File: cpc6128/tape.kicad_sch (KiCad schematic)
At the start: 60 parts, among them IC301 LA4140, IC302 LA6358S, J301 +5V, J306 TAPE_PORT, Q101 2SC2120Y, Q301 KTC1815Y, Q302 Q_NPN_ECB, Q303 Q_PNP_ECB

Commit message: Update title blocks
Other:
- company: (none) -> Amstrad plc
- title: Tape/Sound/Power -> CPC6128 MC0020x tape audio and power
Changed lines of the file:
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@@
   (paper "A3")
   (title_block
-    (title "Tape/Sound/Power")
+    (title "CPC6128 MC0020x tape audio and power")
+    (date "2022-08-20")
+    (rev "1")
+    (company "Amstrad plc")
   )
   (junction (at 83.82 104.775) (diameter 0) (color 0 0 0 0)

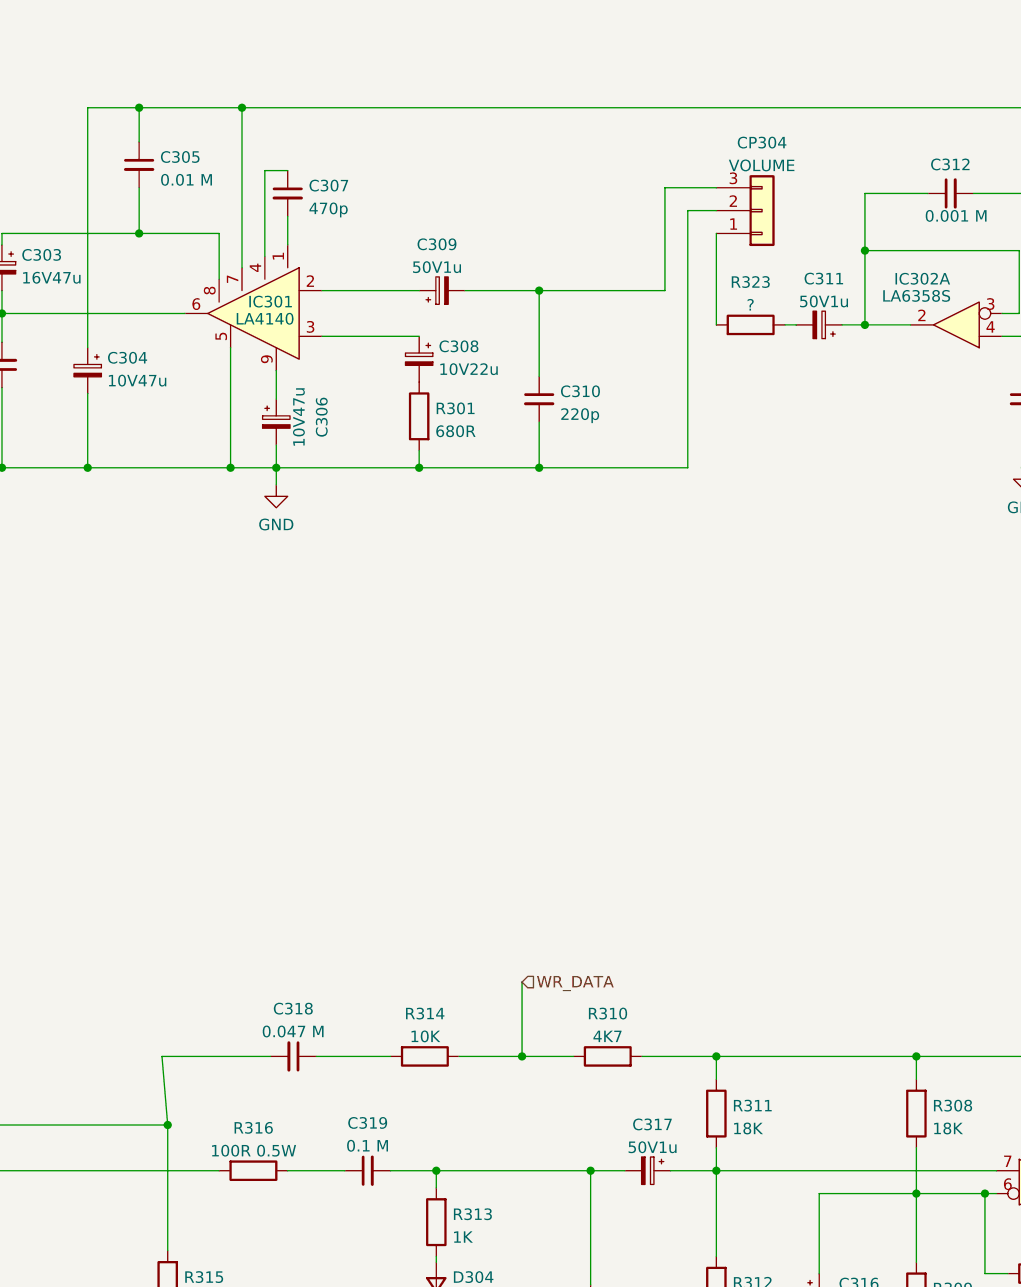
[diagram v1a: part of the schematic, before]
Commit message: Fixes from new top pcb image
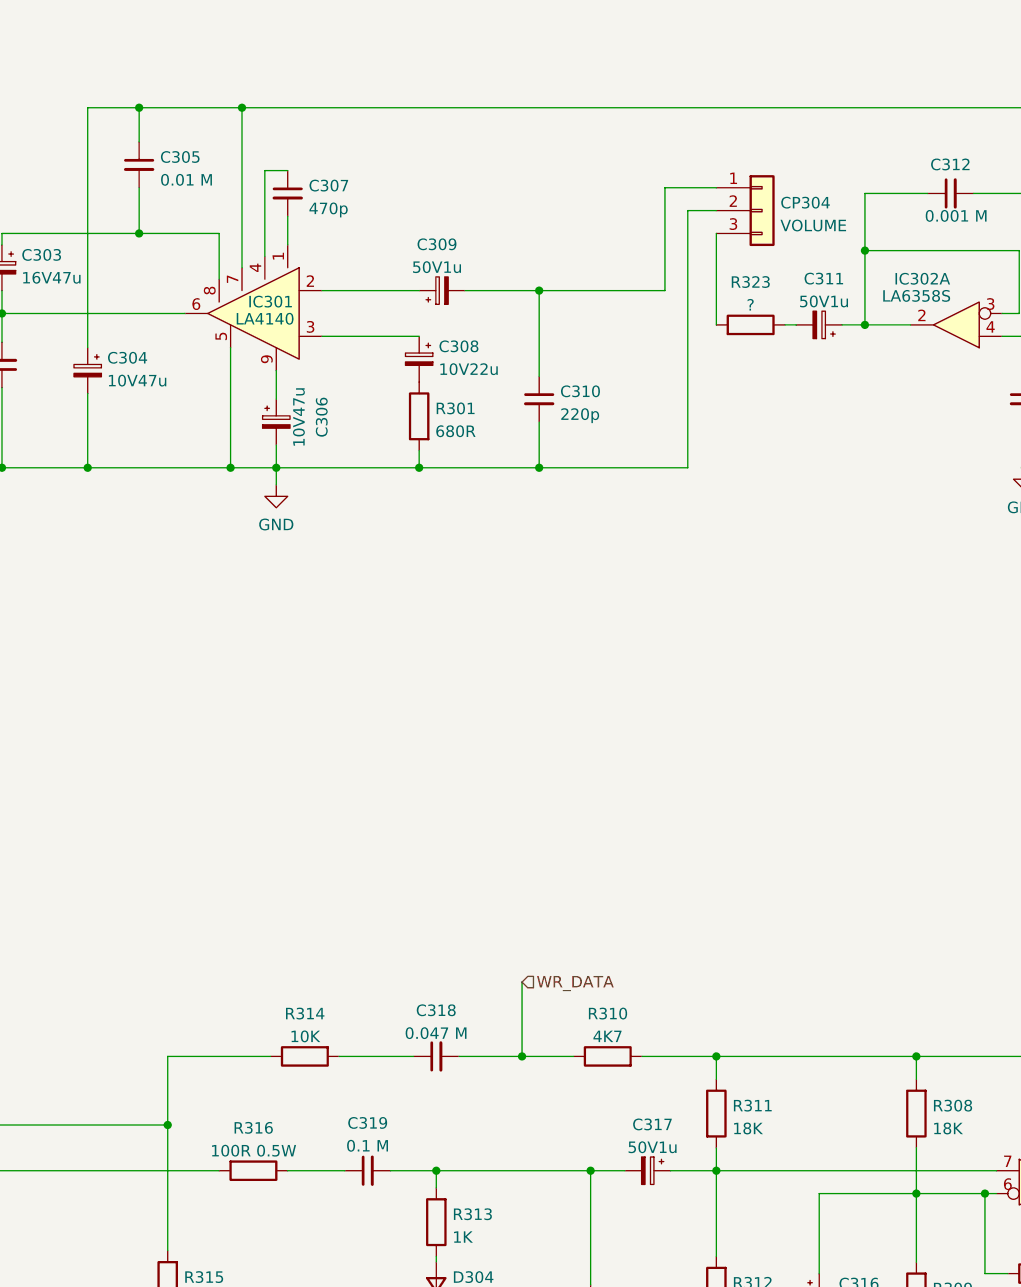
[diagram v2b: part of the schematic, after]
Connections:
- net EAR: now also R314.1; no longer C318.2
- net WR_DATA: now also C318.2; no longer R314.1
- net at C309.2, C310.1: now also CP304.1 (Pin_1); no longer CP304.3 (Pin_3)
- net at R323.2: now also CP304.3 (Pin_3); no longer CP304.1 (Pin_1)
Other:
- moved on the sheet: C318, R314
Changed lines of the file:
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@@
     (stroke (width 0) (type default) (color 0 0 0 0))
   )
-  (wire (pts (xy 109.22 170.18) (xy 117.475 170.18))
+  (wire (pts (xy 111.76 170.18) (xy 120.015 170.18))
     (stroke (width 0) (type default) (color 0 0 0 0))
   )
@@
     (stroke (width 0) (type default) (color 0 0 0 0))
   )
+  (wire (pts (xy 92.71 170.18) (xy 104.14 170.18))
+    (stroke (width 0) (type default) (color 0 0 0 0))
+  )
   (wire (pts (xy 153.67 182.88) (xy 153.67 192.405))
     (stroke (width 0) (type default) (color 0 0 0 0))
@@
     (stroke (width 0) (type default) (color 0 0 0 0))
   )
-  (wire (pts (xy 92.71 177.8) (xy 92.075 170.18))
+  (wire (pts (xy 92.71 177.8) (xy 92.71 170.18))
     (stroke (width 0) (type default) (color 0 0 0 0))
   )
@@
   )
   (wire (pts (xy 43.815 195.58) (xy 43.815 201.93))
-    (stroke (width 0) (type default) (color 0 0 0 0))
-  )
-  (wire (pts (xy 92.075 170.18) (xy 104.14 170.18))
     (stroke (width 0) (type default) (color 0 0 0 0))
   )
@@
     (pin "1")
   )
-  (symbol (lib_id "Device:R") (at 121.285 170.18 270) (unit 1)
-    (in_bom yes) (on_board yes) (fields_autoplaced)
-    (property "Reference" "R314" (id 0) (at 121.285 165.4642 90))
-    (property "Value" "10K" (id 1) (at 121.285 168.0011 90))
-    (property "Footprint" "Resistor_THT:R_Axial_DIN0207_L6.3mm_D2.5mm_P10.16mm_Horizontal" (id 2) (at 121.285 168.402 90)
-      (effects (font (size 1.27 1.27)) hide)
-    )
-    (property "Datasheet" "~" (id 3) (at 121.285 170.18 0)
+  (symbol (lib_id "Device:R") (at 107.95 170.18 90) (mirror x) (unit 1)
+    (in_bom yes) (on_board yes) (fields_autoplaced)
+    (property "Reference" "R314" (id 0) (at 107.95 165.4642 90))
+    (property "Value" "10K" (id 1) (at 107.95 168.0011 90))
+    (property "Footprint" "Resistor_THT:R_Axial_DIN0207_L6.3mm_D2.5mm_P10.16mm_Horizontal" (id 2) (at 107.95 168.402 90)
+      (effects (font (size 1.27 1.27)) hide)
+    )
+    (property "Datasheet" "~" (id 3) (at 107.95 170.18 0)
       (effects (font (size 1.27 1.27)) hide)
     )
@@
     (pin "1")
   )
-  (symbol (lib_id "Device:C_Small") (at 106.68 170.18 270) (unit 1)
+  (symbol (lib_id "Device:C_Small") (at 122.555 170.18 90) (unit 1)
     (in_bom yes) (on_board yes)
-    (property "Reference" "C318" (id 0) (at 106.6736 164.9181 90))
-    (property "Value" "0.047 M" (id 1) (at 106.6736 167.455 90))
-    (property "Footprint" "Capacitor_THT:C_Rect_L7.0mm_W2.0mm_P5.00mm" (id 2) (at 106.68 170.18 0)
-      (effects (font (size 1.27 1.27)) hide)
-    )
-    (property "Datasheet" "~" (id 3) (at 106.68 170.18 0)
+    (property "Reference" "C318" (id 0) (at 122.555 165.1 90))
+    (property "Value" "0.047 M" (id 1) (at 122.555 167.64 90))
+    (property "Footprint" "Capacitor_THT:C_Rect_L7.0mm_W2.0mm_P5.00mm" (id 2) (at 122.555 170.18 0)
+      (effects (font (size 1.27 1.27)) hide)
+    )
+    (property "Datasheet" "~" (id 3) (at 122.555 170.18 0)
       (effects (font (size 1.27 1.27)) hide)
     )
@@
     (pin "2")
   )
-  (symbol (lib_id "Connector_Generic:Conn_01x03") (at 158.75 76.2 0) (mirror x) (unit 1)
-    (in_bom yes) (on_board yes) (fields_autoplaced)
-    (property "Reference" "CP304" (id 0) (at 158.75 68.6902 0))
-    (property "Value" "VOLUME" (id 1) (at 158.75 71.2271 0))
+  (symbol (lib_id "Connector_Generic:Conn_01x03") (at 158.75 76.2 0) (unit 1)
+    (in_bom yes) (on_board yes) (fields_autoplaced)
+    (property "Reference" "CP304" (id 0) (at 160.782 75.3653 0)
+      (effects (font (size 1.27 1.27)) (justify left))
+    )
+    (property "Value" "VOLUME" (id 1) (at 160.782 77.9022 0)
+      (effects (font (size 1.27 1.27)) (justify left))
+    )
     (property "Footprint" "Connector_Molex:Molex_KK-254_AE-6410-03A_1x03_P2.54mm_Vertical" (id 2) (at 158.75 76.2 0)
       (effects (font (size 1.27 1.27)) hide)

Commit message: Minor cleanups
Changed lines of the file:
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@@
     (effects (font (size 1.27 1.27)) (justify left))
   )
-  (hierarchical_label "RD_DATA" (shape input) (at 198.12 184.15 0)
+  (hierarchical_label "RD_DATA" (shape output) (at 198.12 184.15 0)
     (effects (font (size 1.27 1.27)) (justify left))
   )

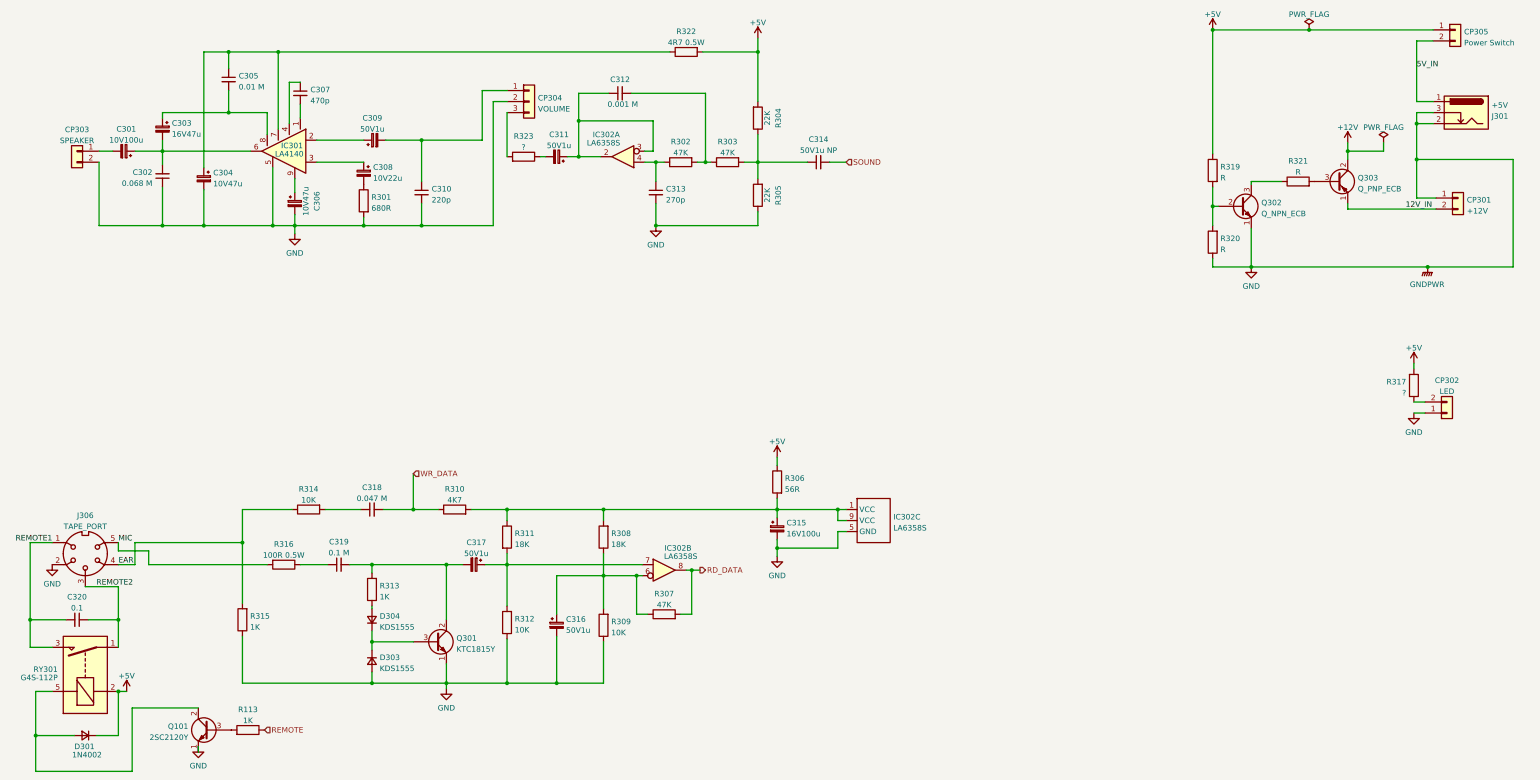
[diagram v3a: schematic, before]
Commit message: Correct C136 (missing) and C314 (wrong footprint) Thanks @orzel!
Also migrated to KiCad 9.
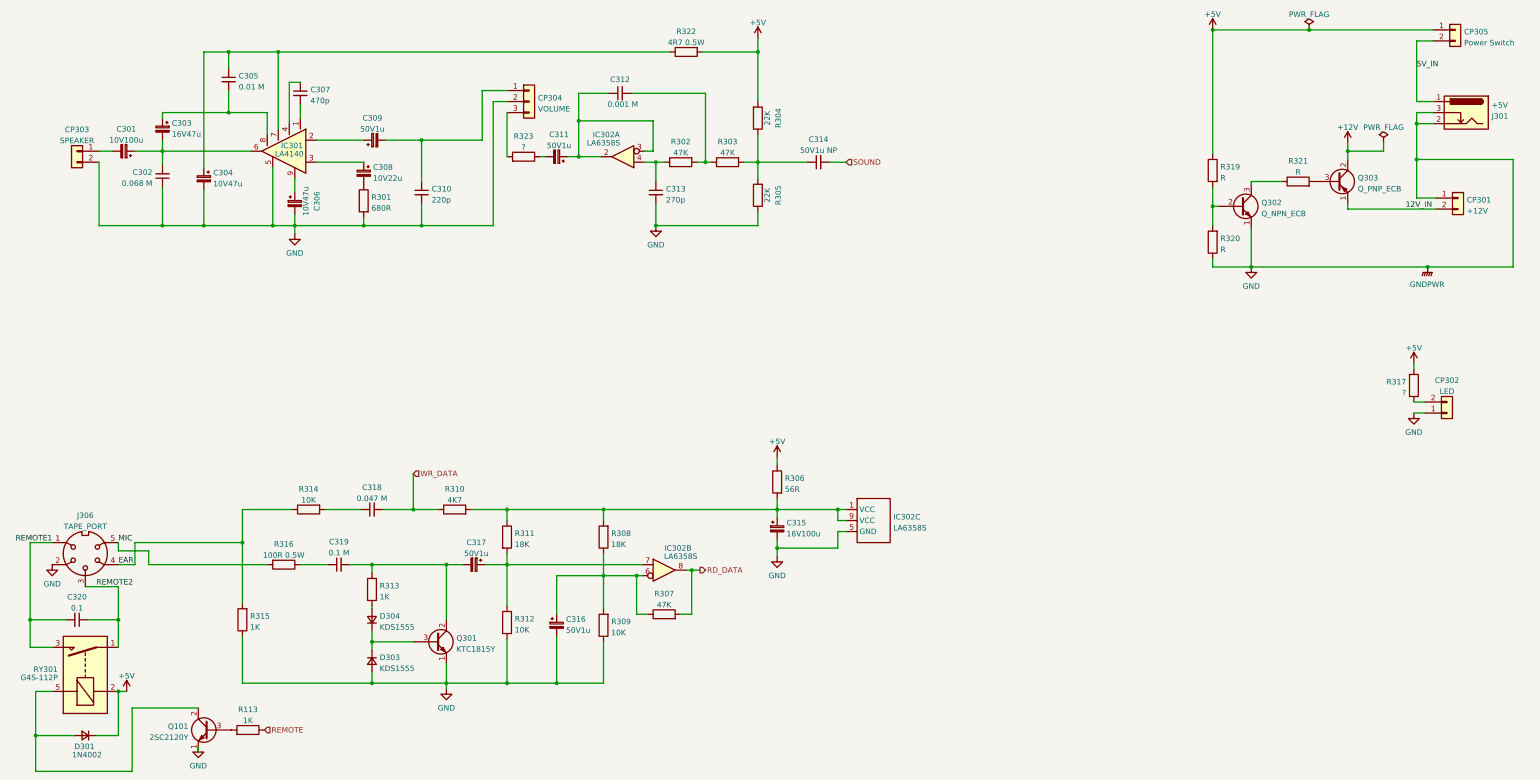
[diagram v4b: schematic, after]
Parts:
- C314: footprint Capacitor_THT:C_Disc_D4.3mm_W1.9mm_P5.00mm -> Amstrad-CPC:C_Radial_D4.0mm_P5.00mm
